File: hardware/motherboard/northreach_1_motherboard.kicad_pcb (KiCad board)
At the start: 2 copper layers, 41 x 96 mm, 21 parts, among them J1 USB_C_Receptacle, J2 Conn_01x03_Pin, J3 Conn_01x20, J4 Conn_01x03_Pin, SW1 SW_Push, SW2 SW_Push, U1 TPS7A4701xRGW, U2 ESP32-S3-MINI-1U

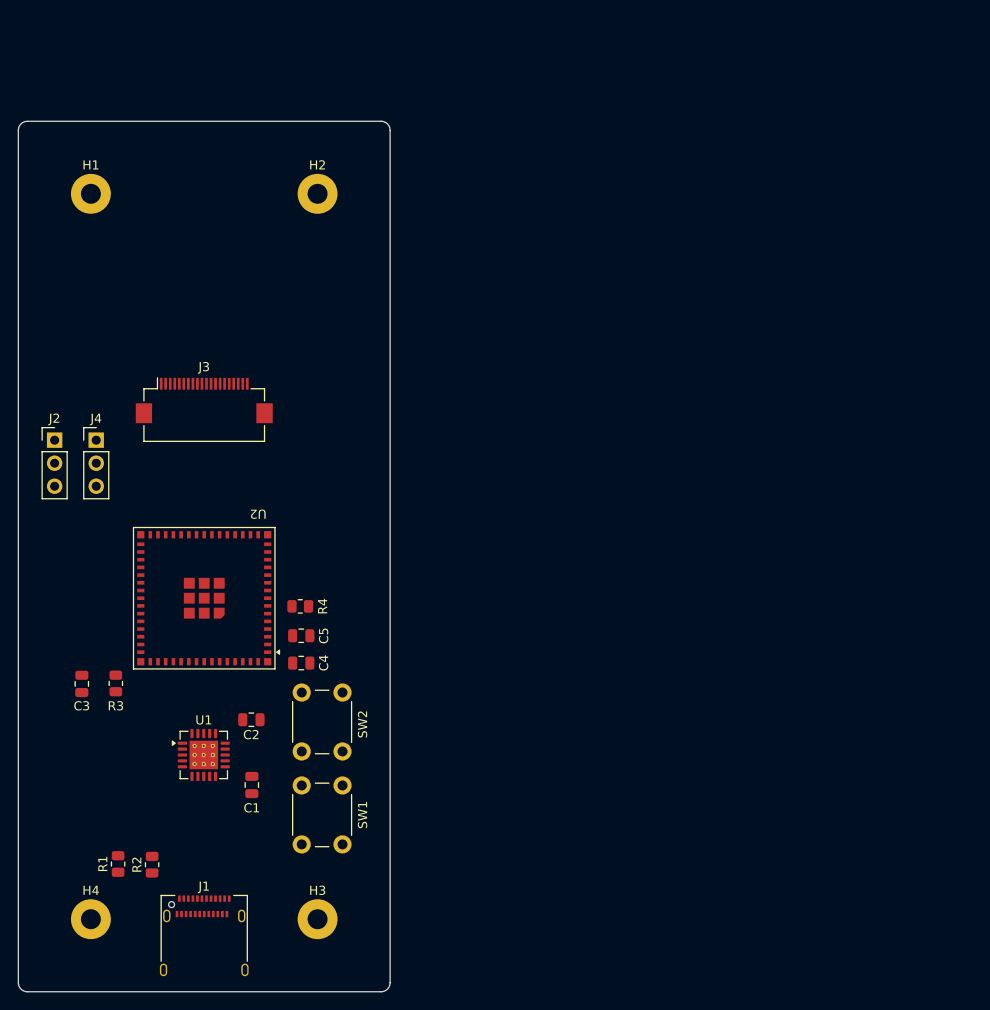
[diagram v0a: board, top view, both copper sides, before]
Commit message: pcb: motherboard: route stuff
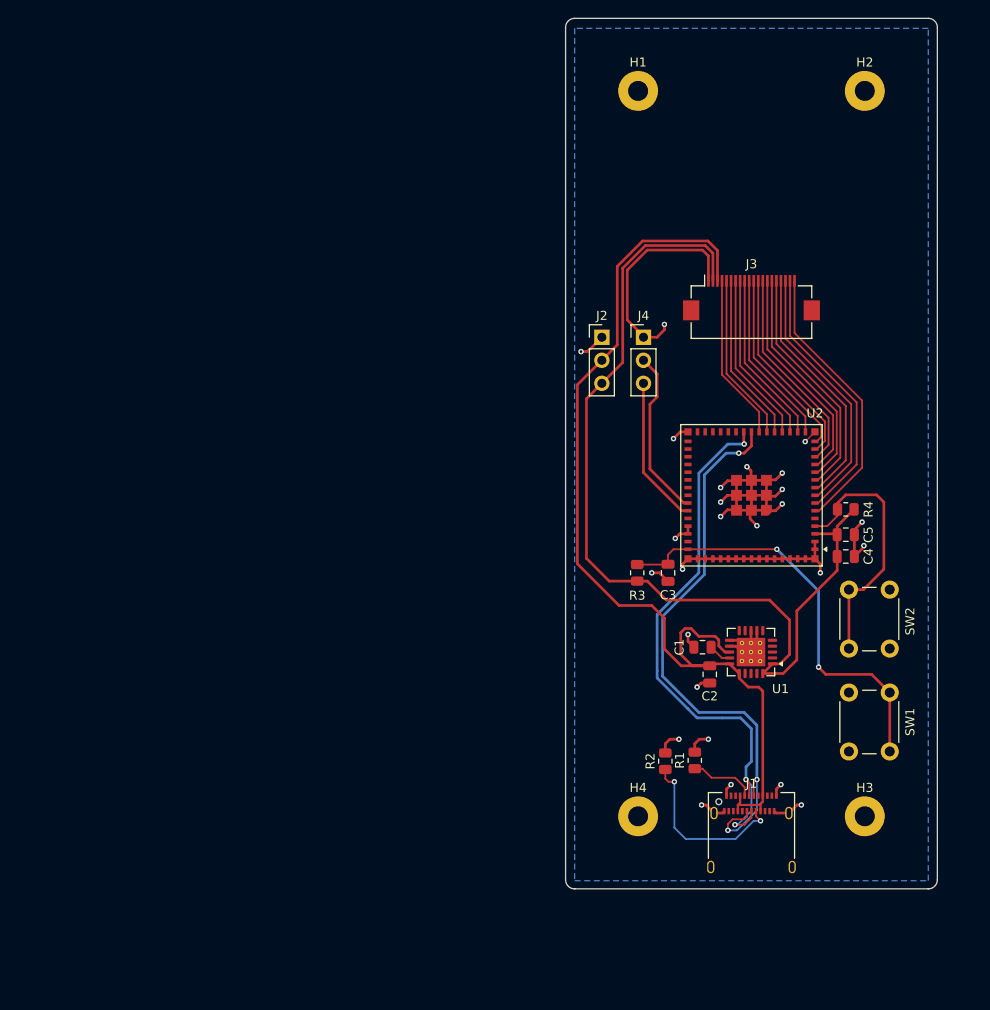
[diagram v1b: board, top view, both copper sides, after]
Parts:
- moved C3 65.8 mm to (140.2, 106.0)
- moved R1 64.6 mm to (143.1, 126.7)
- moved U1 61.4 mm to (149.3, 114.8), turned to 180 degrees
- moved H1 61.4 mm to (136.8, 52.9)
- moved H2 61.4 mm to (161.8, 52.9)
- moved H3 61.4 mm to (161.8, 132.9)
- moved H4 61.4 mm to (136.8, 132.9)
- moved J1 61.4 mm to (149.3, 135.7)
- moved J2 61.4 mm to (132.8, 80.1)
- moved J3 61.4 mm to (149.3, 75.7)
- moved J4 61.4 mm to (137.4, 80.1)
- moved SW2 61.4 mm to (164.6, 107.9)
- moved U2 61.4 mm to (149.3, 97.5)
- moved SW1 61.2 mm to (160.1, 125.8)
- moved C4 61.2 mm to (159.8, 104.2)
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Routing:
- net GND: track 0.00 -> 118.7 mm, vias 0 -> 26
- net VBUS: track 0.00 -> 110.2 mm
- net VDD: track 0.00 -> 107.0 mm
- net USB_D_NEGATIVE: track 0.00 -> 64.0 mm, vias 0 -> 3
- net USB_D_POSITIVE: track 0.00 -> 61.9 mm, vias 0 -> 3
- net MCU_EN: track 0.00 -> 47.1 mm, vias 0 -> 2
- net Net-(J3-Pin_20): track 0.00 -> 30.9 mm
- net Net-(J3-Pin_19): track 0.00 -> 29.7 mm
- net MCU_BOOT: track 0.00 -> 28.9 mm
- net Net-(J3-Pin_18): track 0.00 -> 28.5 mm
- net Net-(J3-Pin_17): track 0.00 -> 27.4 mm
- net Net-(J3-Pin_16): track 0.00 -> 26.2 mm
- net Net-(J3-Pin_15): track 0.00 -> 25.3 mm
- net Net-(J3-Pin_14): track 0.00 -> 24.3 mm
- net Net-(J3-Pin_13): track 0.00 -> 23.1 mm
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- added copper zone on B.Cu, net GND

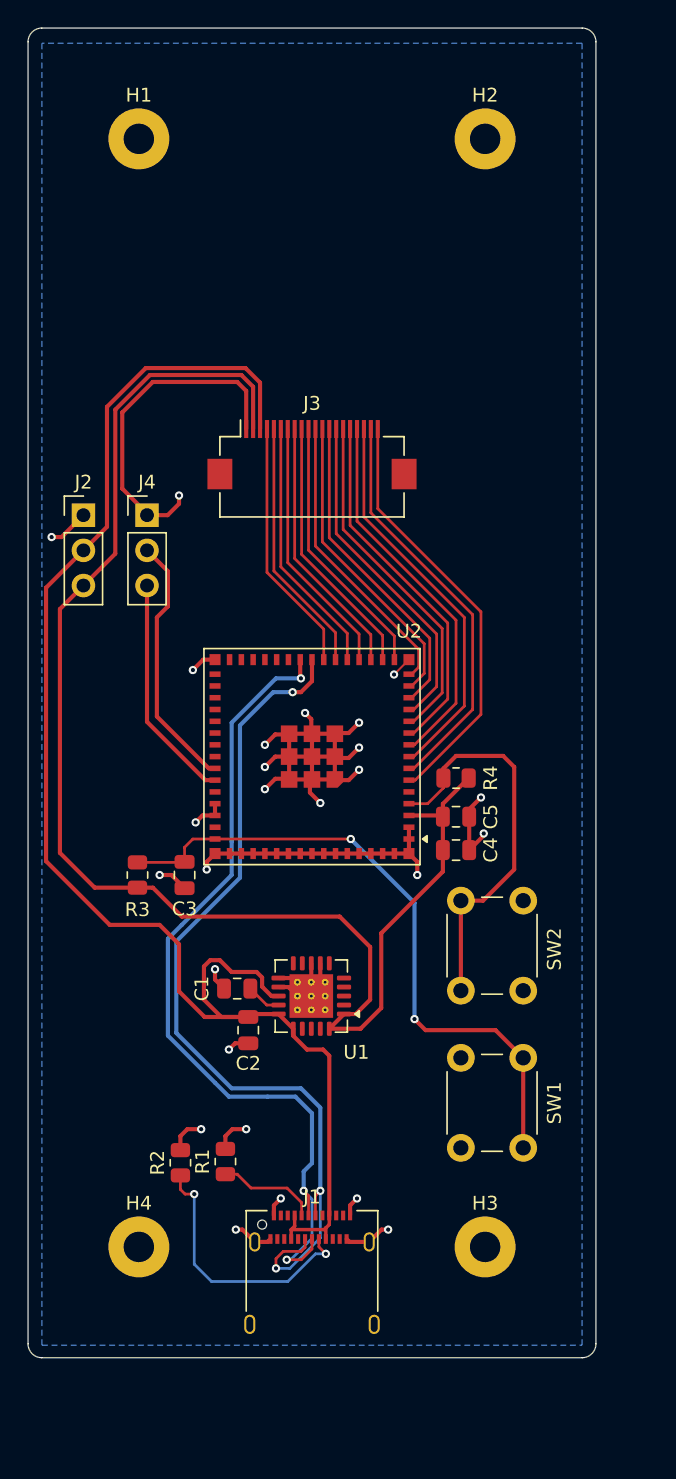
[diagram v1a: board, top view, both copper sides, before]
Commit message: pcb: motherboard: silkscreen
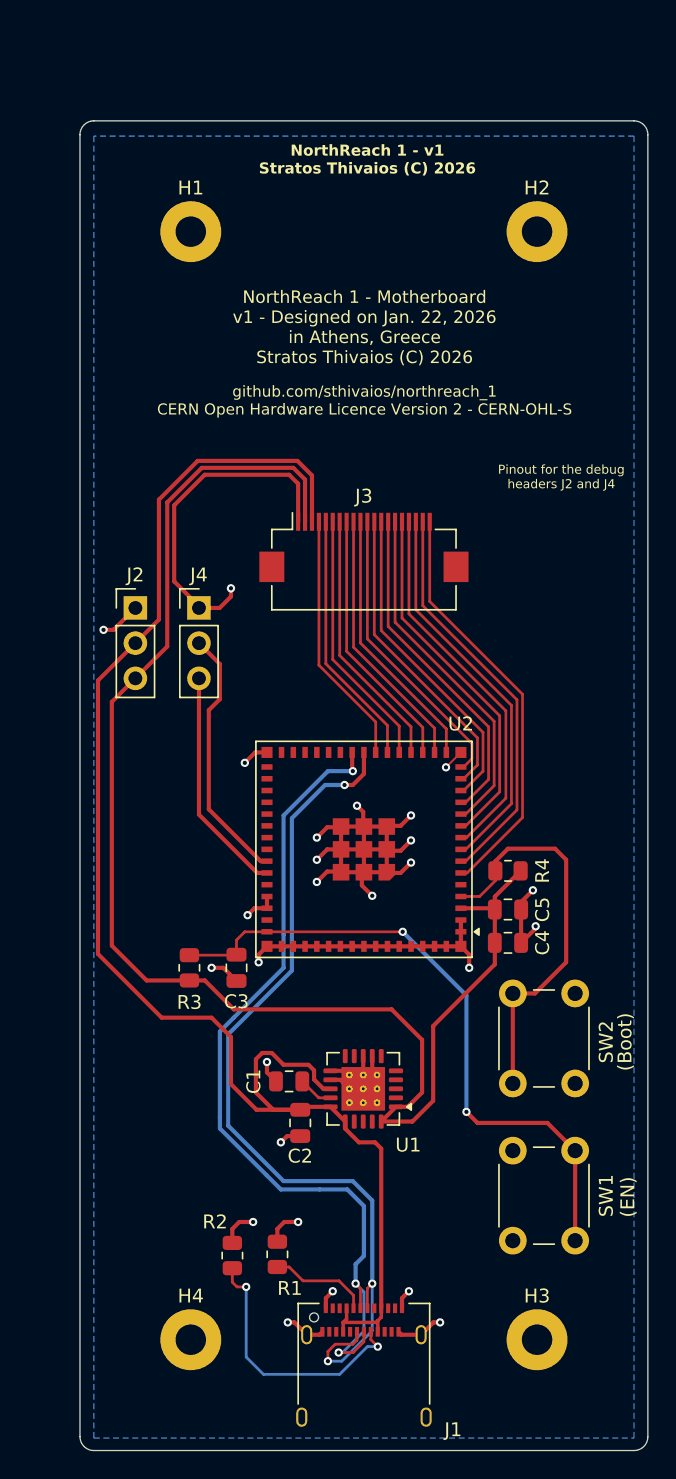
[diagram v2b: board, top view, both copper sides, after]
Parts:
- moved C1 7.68 mm to (147.7, 121.0)
- moved C2 7.68 mm to (148.5, 124.0)
- moved C3 7.68 mm to (143.9, 112.8)
- moved C4 7.68 mm to (163.5, 111.0)
- moved C5 7.68 mm to (163.5, 108.5)
- moved H1 7.68 mm to (140.6, 59.6)
- moved H2 7.68 mm to (165.6, 59.6)
- moved J2 7.68 mm to (136.6, 86.8)
- moved J3 7.68 mm to (153.1, 82.4)
- moved J4 7.68 mm to (141.2, 86.8)
- moved R1 7.68 mm to (146.8, 133.4)
- moved R2 7.68 mm to (143.6, 133.5)
- moved R3 7.68 mm to (140.5, 112.8)
- moved R4 7.68 mm to (163.5, 105.8)
- moved U1 7.68 mm to (153.1, 121.5)
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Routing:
- net Net-(J3-Pin_20): track 30.9 -> 30.2 mm
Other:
- board text added: "(Boot)"
- board text added: "(EN)"
- board text added: "NorthReach 1 - Motherboard v1 - Designed on Jan. 22, 2026 in Athens, Greece Stratos Thivaios (C) 2026"
- board text added: "NorthReach 1 - v1 Stratos Thivaios (C) 2026"
- board text added: "Pinout for the debug headers J2 and J4"
- board text added: "github.com/sthivaios/northreach_1 CERN Open Hardware Licence Version 2 - CERN-OHL-S"

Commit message: pcb: motherboard: add ESD protection
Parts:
- added U3: USBLC6-2SC6, Package_TO_SOT_SMD:SOT-23-6, F.Cu at (153.6, 133.7)
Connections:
- J1 pad A6: USB_D_POSITIVE -> Net-(J1-D+-PadA6)
- J1 pad A7: USB_D_NEGATIVE -> Net-(J1-D--PadA7)
- J1 pad B6: USB_D_POSITIVE -> Net-(J1-D+-PadA6)
- J1 pad B7: USB_D_NEGATIVE -> Net-(J1-D--PadA7)
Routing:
- net USB_D_NEGATIVE: track 64.0 -> 49.1 mm, vias 3 -> 2
- net USB_D_POSITIVE: track 61.9 -> 49.0 mm, vias 3 -> 2
- net Net-(J1-D+-PadA6): track 0.00 -> 9.39 mm, vias 0 -> 2
- net VBUS: track 110.2 -> 119.3 mm
- net Net-(J1-D--PadA7): track 0.00 -> 8.37 mm, vias 0 -> 2
- net GND: track 118.7 -> 121.3 mm, vias 26 -> 27
- net Net-(J1-CC2): track 19.3 -> 18.5 mm

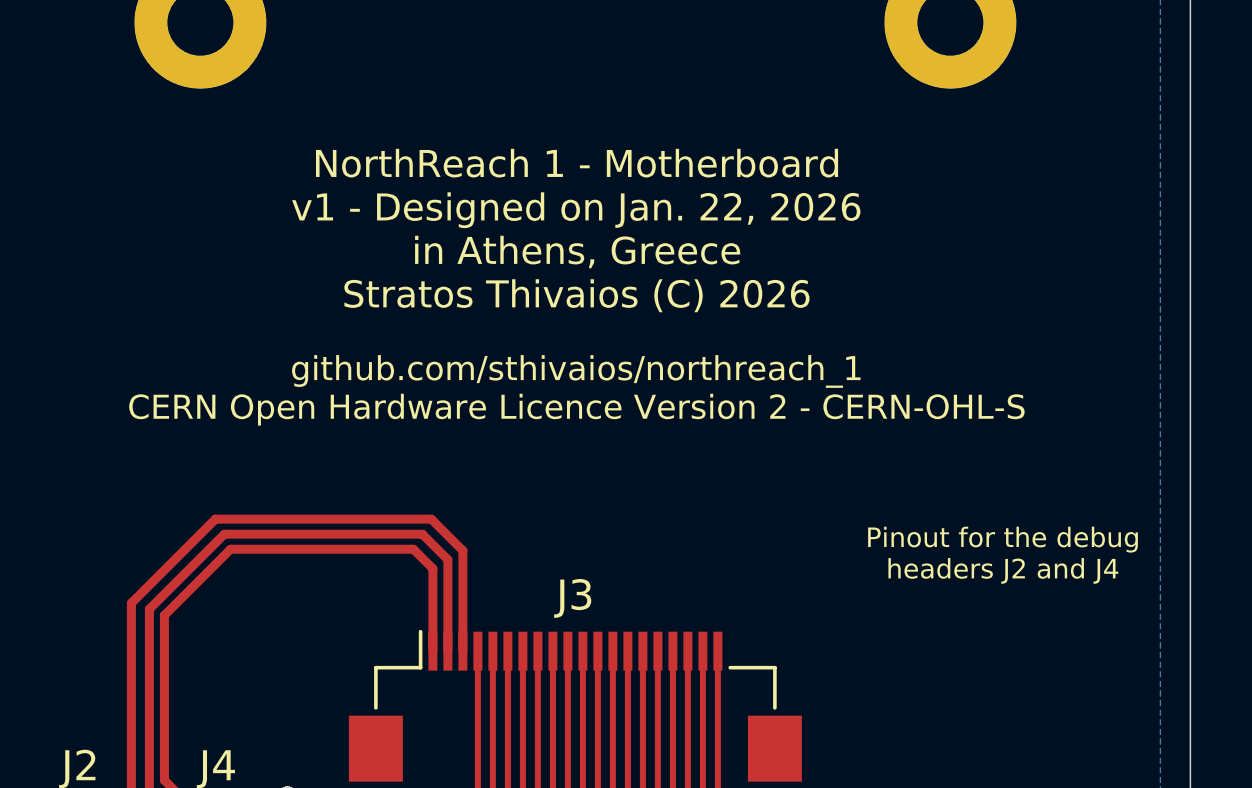
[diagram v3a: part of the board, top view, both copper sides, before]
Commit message: pcb: motherboard: fix silkscreen stuff
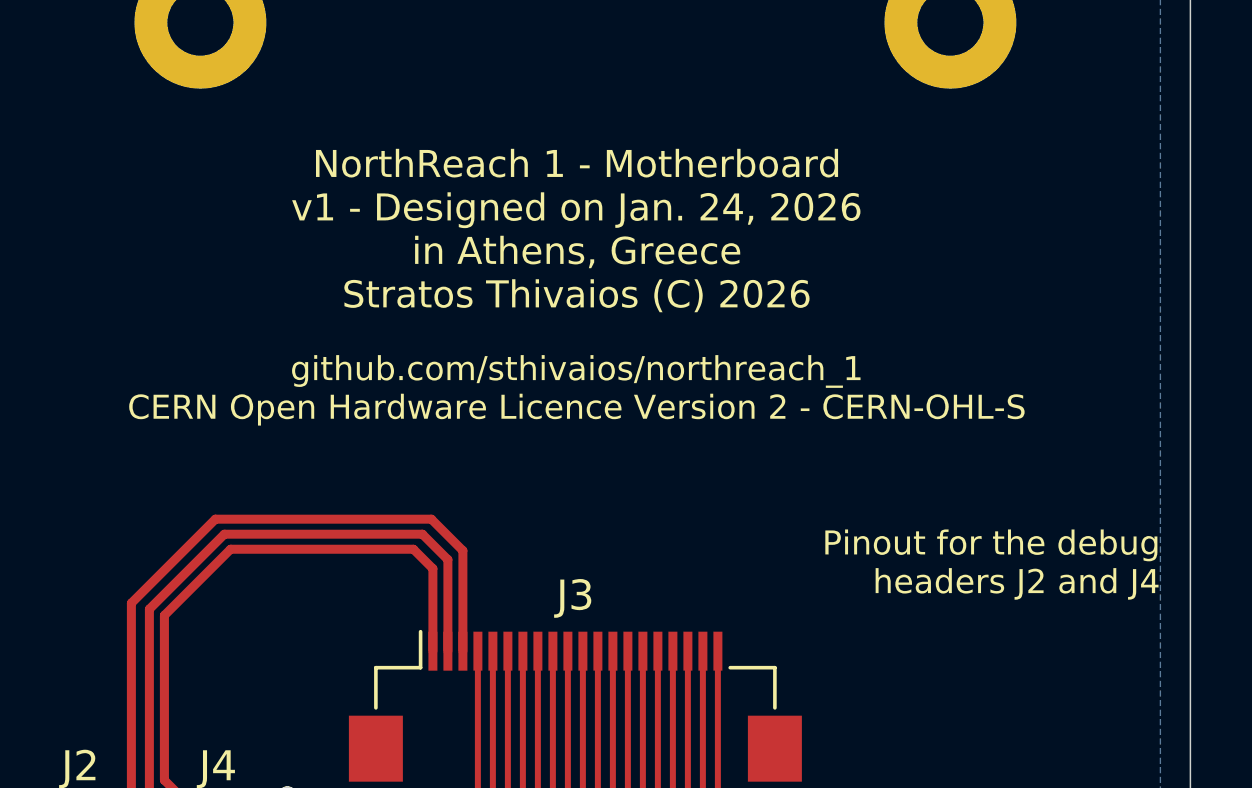
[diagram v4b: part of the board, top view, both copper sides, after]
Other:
- board text added: "NorthReach 1 - Motherboard v1 - Designed on Jan. 24, 2026 in Athens, Greece Stratos Thivaios (C) 2026"
- board text removed: "NorthReach 1 - Motherboard v1 - Designed on Jan. 22, 2026 in Athens, Greece Stratos Thivaios (C) 2026"
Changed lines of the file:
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@@
 	(title_block
 		(title "NorthReach 1 - Motherboard")
-		(date "2026-01-22")
+		(date "2026-01-24")
 		(rev "v1.0")
 		(company "Stratos Thivaios")
@@
 		(layer "Edge.Cuts")
 	)
-	(gr_text "NorthReach 1 - Motherboard\nv1 - Designed on Jan. 22, 2026\nin Athens, Greece\nStratos Thivaios (C) 2026"
+	(gr_text "NorthReach 1 - Motherboard\nv1 - Designed on Jan. 24, 2026\nin Athens, Greece\nStratos Thivaios (C) 2026"
 		(at 153.15 69.2 0)
 		(layer "F.SilkS")
@@
 	)
 	(gr_text "Pinout for the debug\nheaders J2 and J4"
-		(at 167.35 77.3 0)
+		(at 172.6 77.6 0)
 		(layer "F.SilkS")
 		(effects
 			(font
-				(size 0.65 0.65)
+				(size 0.8 0.8)
 				(thickness 0.1)
 			)
+			(justify right)
 		)
 	)
@@
 		)
 		(column_widths 3.825 5.8)
-		(row_heights 2.25 2 2 2)
+		(row_heights 3 2 2 2)
 		(cells
 			(table_cell "J2"
-				(start 162.5375 78.575)
-				(end 166.3625 80.825)
+				(start 162.7875 79.4)
+				(end 166.6125 82.4)
 				(margins 1.0025 1.0025 1.0025 1.0025)
 				(span 1 1)
@@
 				(effects
 					(font
-						(size 1 1)
+						(size 0.8 0.8)
+						(thickness 0.15)
 					)
 				)
 			)
 			(table_cell "J4 (UART)"
-				(start 166.3625 78.575)
-				(end 172.1625 80.825)
+				(start 166.6125 79.4)
+				(end 172.4125 82.4)
 				(margins 1.0025 1.0025 1.0025 1.0025)
 				(span 1 1)
@@
 				(effects
 					(font
-						(size 0.6 0.6)
+						(size 0.8 0.8)
+						(thickness 0.15)
 					)
 				)
 			)
 			(table_cell "GND"
-				(start 162.5375 80.825)
-				(end 166.3625 82.825)
+				(start 162.7875 82.4)
+				(end 166.6125 84.4)
 				(margins 1.0025 1.0025 1.0025 1.0025)
 				(span 1 1)
@@
 				(effects
 					(font
-						(size 0.7 0.7)
+						(size 0.8 0.8)
+						(thickness 0.08)
 					)
 				)
 			)
 			(table_cell "GND"
-				(start 166.3625 80.825)
-				(end 172.1625 82.825)
+				(start 166.6125 82.4)
+				(end 172.4125 84.4)
 				(margins 1.0025 1.0025 1.0025 1.0025)
 				(span 1 1)
@@
 				(effects
 					(font
-						(size 0.7 0.7)
+						(size 0.8 0.8)
+						(thickness 0.08)
 					)
 				)
 			)
 			(table_cell "VBUS"
-				(start 162.5375 82.825)
-				(end 166.3625 84.825)
+				(start 162.7875 84.4)
+				(end 166.6125 86.4)
 				(margins 1.0025 1.0025 1.0025 1.0025)
 				(span 1 1)
@@
 				(effects
 					(font
-						(size 0.7 0.7)
+						(size 0.8 0.8)
+						(thickness 0.08)
 					)
 				)
 			)
 			(table_cell "UART_TXD"
-				(start 166.3625 82.825)
-				(end 172.1625 84.825)
+				(start 166.6125 84.4)
+				(end 172.4125 86.4)
 				(margins 1.0025 1.0025 1.0025 1.0025)
 				(span 1 1)
@@
 				(effects
 					(font
-						(size 0.7 0.7)
+						(size 0.8 0.75)
+						(thickness 0.08)
 					)
 				)
 			)
 			(table_cell "VDD"
-				(start 162.5375 84.825)
-				(end 166.3625 86.825)
+				(start 162.7875 86.4)
+				(end 166.6125 88.4)
 				(margins 1.0025 1.0025 1.0025 1.0025)
 				(span 1 1)
@@
 				(effects
 					(font
-						(size 0.7 0.7)
+						(size 0.8 0.8)
+						(thickness 0.08)
 					)
 				)
 			)
 			(table_cell "UART_RXD"
-				(start 166.3625 84.825)
-				(end 172.1625 86.825)
+				(start 166.6125 86.4)
+				(end 172.4125 88.4)
 				(margins 1.0025 1.0025 1.0025 1.0025)
 				(span 1 1)
@@
 				(effects
 					(font
-						(size 0.7 0.7)
+						(size 0.8 0.75)
+						(thickness 0.08)
 					)
 				)
@@
 	)
 	(segment
-		(start 155.2 133.6)
-		(end 154.087501 133.6)
-		(width 0.3)
-		(layer "F.Cu")
-		(net 1)
-	)
-	(segment
 		(start 155.81 139.24)
 		(end 155.6 139.03)
@@
 	)
 	(segment
-		(start 153.55 134.137501)
-		(end 153.55 134.8)
+		(start 158.6 138.35)
+		(end 158.12 138.35)
 		(width 0.3)
 		(layer "F.Cu")
@@
 	)
 	(segment
-		(start 158.6 138.35)
-		(end 158.12 138.35)
+		(start 154.087501 133.6)
+		(end 153.55 134.137501)
 		(width 0.3)
 		(layer "F.Cu")
@@
 	)
 	(segment
-		(start 154.087501 133.6)
-		(end 153.55 134.137501)
-		(width 0.3)
-		(layer "F.Cu")
-		(net 1)
-	)
-	(segment
 		(start 164.45 108.54)
 		(end 164.45 108)
@@
 	)
 	(segment
+		(start 153.55 134.137501)
+		(end 153.55 134.8)
+		(width 0.3)
+		(layer "F.Cu")
+		(net 1)
+	)
+	(segment
 		(start 135.02 88.35)
 		(end 136.6 86.77)
@@
 		(width 0.3)
 		(layer "F.Cu")
+		(net 1)
+	)
+	(segment
+		(start 155.2 133.6)
+		(end 154.087501 133.6)
+		(width 0.3)
+		(layer "F.Cu")
